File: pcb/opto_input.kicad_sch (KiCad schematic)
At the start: 6 parts, among them J33 Screw_Terminal_01x02, U9 VO615A

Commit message: Use larger screw terminals, adjust layout to suit
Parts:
- J33: footprint Conn_ScrewTerminals:ED5552DS -> Conn_ScrewTerminals:CTB7000-2
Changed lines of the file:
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@@
 	(label "COM"
 		(at 97.79 78.74 270)
-		(fields_autoplaced yes)
 		(effects
 			(font
@@
 	(label "SIG"
 		(at 97.79 76.2 90)
-		(fields_autoplaced yes)
 		(effects
 			(font
@@
 		(shape output)
 		(at 203.2 81.28 0)
-		(fields_autoplaced yes)
 		(effects
 			(font
@@
 			)
 		)
-		(property "Footprint" "Conn_ScrewTerminals:ED5552DS"
+		(property "Footprint" "Conn_ScrewTerminals:CTB7000-2"
 			(at 83.82 78.74 0)
 			(effects

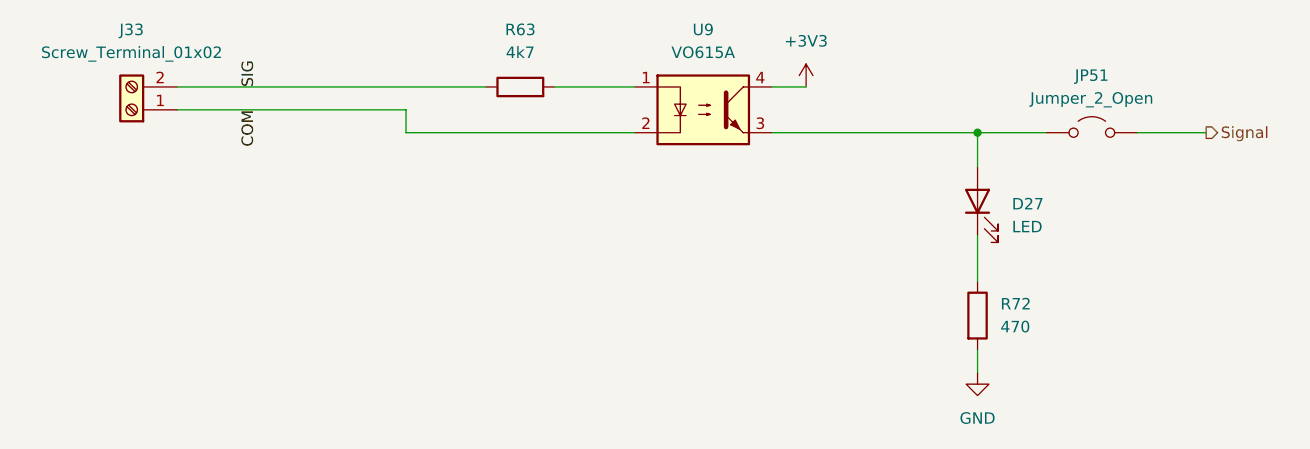
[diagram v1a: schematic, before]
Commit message: Convert PCB to KiCad 9 project
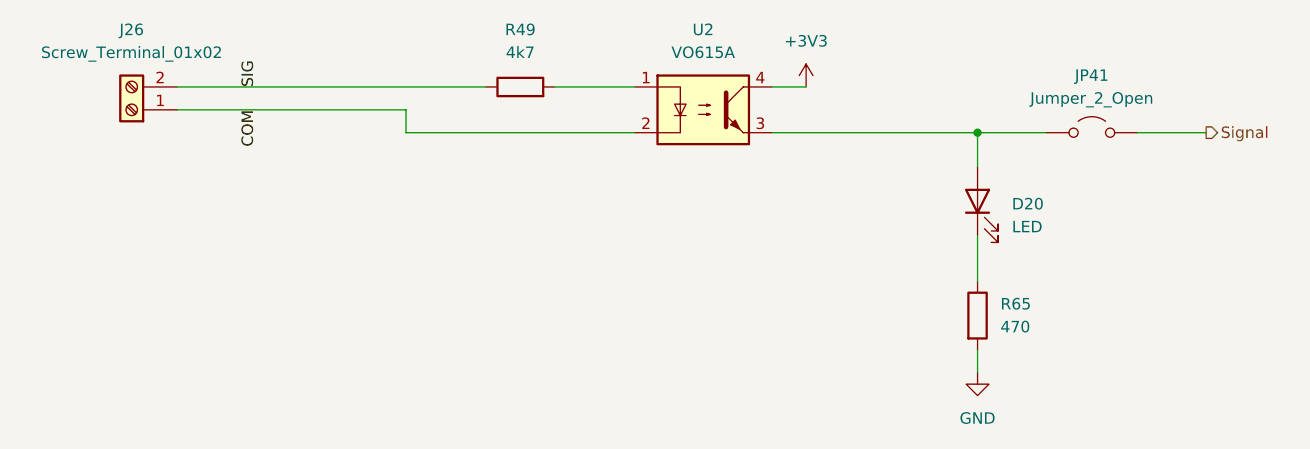
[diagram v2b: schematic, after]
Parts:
- renumbered D27 to D20, J33 to J26, JP51 to JP41, R63 to R49, R72 to R65, U9 to U2
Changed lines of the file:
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@@
 (kicad_sch
-	(version 20231120)
+	(version 20250114)
 	(generator "eeschema")
-	(generator_version "8.0")
+	(generator_version "9.0")
 	(paper "A4")
 	(junction
@@
 		(dnp no)
 		(fields_autoplaced yes)
-		(property "Reference" "JP51"
+		(property "Reference" "JP41"
 			(at 190.5 74.93 0)
 			(effects
@@
 		(dnp no)
 		(fields_autoplaced yes)
-		(property "Reference" "#PWR0131"
+		(property "Reference" "#PWR0103"
 			(at 177.8 114.3 0)
 			(effects
@@
 		(dnp no)
 		(fields_autoplaced yes)
-		(property "Reference" "R72"
+		(property "Reference" "R65"
 			(at 180.34 100.3299 0)
 			(effects
@@
 		(dnp no)
 		(fields_autoplaced yes)
-		(property "Reference" "#PWR0130"
+		(property "Reference" "#PWR0102"
 			(at 158.75 80.01 0)
 			(effects
@@
 		(dnp no)
 		(fields_autoplaced yes)
-		(property "Reference" "J33"
+		(property "Reference" "J26"
 			(at 83.82 69.85 0)
 			(effects
@@
 		(dnp no)
 		(fields_autoplaced yes)
-		(property "Reference" "R63"
+		(property "Reference" "R49"
 			(at 127 69.85 90)
 			(effects
@@
 		(dnp no)
 		(fields_autoplaced yes)
-		(property "Reference" "U9"
+		(property "Reference" "U2"
 			(at 147.32 69.85 0)
 			(effects
@@
 		(dnp no)
 		(fields_autoplaced yes)
-		(property "Reference" "D27"
+		(property "Reference" "D20"
 			(at 181.61 89.2174 90)
 			(effects
